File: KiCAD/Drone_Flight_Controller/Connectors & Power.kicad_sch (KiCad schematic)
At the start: 10 parts, among them J1 XT60, P1 USB_C_Plug_USB2.0, U4 AS358, U5 AS358

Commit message: Fix Bugs
Fix Bugs
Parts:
- removed U5: AS358, Package_SO:SO-8_3.9x4.9mm_P1.27mm, symbol Device:Opamp_Dual
- added U6: AS358, Package_SO:SO-8_3.9x4.9mm_P1.27mm, symbol Device:Opamp_Dual
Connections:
- net +14.8V: now also U6.8 (V+)
- net GND: now also U6.4 (V-)
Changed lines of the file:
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@@
+	)
+	(junction
+		(at 73.66 76.2)
+		(diameter 0)
+		(color 0 0 0 0)
 	)
 	(junction
@@
 	(wire
 		(pts
+			(xy 161.29 99.06) (xy 161.29 101.6)
+		)
+		(stroke
+			(width 0)
+			(type default)
+		)
+	)
+	(wire
+		(pts
 			(xy 142.24 81.28) (xy 152.4 81.28)
 		)
@@
 	(wire
 		(pts
+			(xy 161.29 83.82) (xy 161.29 81.28)
+		)
+		(stroke
+			(width 0)
+			(type default)
+		)
+	)
+	(wire
+		(pts
 			(xy 120.65 144.78) (xy 120.65 142.24)
 		)
@@
 	(wire
 		(pts
-			(xy 161.29 101.6) (xy 161.29 99.06)
-		)
-		(stroke
-			(width 0)
-			(type default)
-		)
-	)
-	(wire
-		(pts
 			(xy 71.12 83.82) (xy 73.66 83.82)
 		)
@@
 	(wire
 		(pts
-			(xy 161.29 83.82) (xy 161.29 81.28)
-		)
-		(stroke
-			(width 0)
-			(type default)
-		)
-	)
-	(wire
-		(pts
 			(xy 71.12 93.98) (xy 73.66 93.98)
 		)
@@
 		(pts
 			(xy 130.81 81.28) (xy 142.24 81.28)
+		)
+		(stroke
+			(width 0)
+			(type default)
+		)
+	)
+	(wire
+		(pts
+			(xy 81.28 73.66) (xy 81.28 76.2)
+		)
+		(stroke
+			(width 0)
+			(type default)
+		)
+	)
+	(wire
+		(pts
+			(xy 81.28 76.2) (xy 73.66 76.2)
 		)
 		(stroke
@@
 	)
 	(symbol
+		(lib_id "Device:Opamp_Dual")
+		(at 163.83 91.44 0)
+		(unit 3)
+		(exclude_from_sim no)
+		(in_bom yes)
+		(on_board yes)
+		(dnp no)
+		(fields_autoplaced yes)
+		(property "Reference" "U6"
+			(at 162.56 90.1699 0)
+			(effects
+				(font
+					(size 1.27 1.27)
+				)
+				(justify left)
+			)
+		)
+		(property "Value" "AS358"
+			(at 162.56 92.7099 0)
+			(effects
+				(font
+					(size 1.27 1.27)
+				)
+				(justify left)
+			)
+		)
+		(property "Footprint" "Package_SO:SO-8_3.9x4.9mm_P1.27mm"
+			(at 163.83 91.44 0)
+			(effects
+				(font
+					(size 1.27 1.27)
+				)
+				(hide yes)
+			)
+		)
+		(property "Datasheet" "~"
+			(at 163.83 91.44 0)
+			(effects
+				(font
+					(size 1.27 1.27)
+				)
+				(hide yes)
+			)
+		)
+		(property "Description" "Dual operational amplifier"
+			(at 163.83 91.44 0)
+			(effects
+				(font
+					(size 1.27 1.27)
+				)
+				(hide yes)
+			)
+		)
+		(property "Sim.Library" "${KICAD9_SYMBOL_DIR}/Simulation_SPICE.sp"
+			(at 163.83 91.44 0)
+			(effects
+				(font
+					(size 1.27 1.27)
+				)
+				(hide yes)
+			)
+		)
+		(property "Sim.Name" "kicad_builtin_opamp_dual"
+			(at 163.83 91.44 0)
+			(effects
+				(font
+					(size 1.27 1.27)
+				)
+				(hide yes)
+			)
+		)
+		(property "Sim.Device" "SUBCKT"
+			(at 163.83 91.44 0)
+			(effects
+				(font
+					(size 1.27 1.27)
+				)
+				(hide yes)
+			)
+		)
+		(property "Sim.Pins" "1=out1 2=in1- 3=in1+ 4=vee 5=in2+ 6=in2- 7=out2 8=vcc"
+			(at 163.83 91.44 0)
+			(effects
+				(font
+					(size 1.27 1.27)
+				)
+				(hide yes)
+			)
+		)
+		(property "Link" "https://www.mouser.at/ProductDetail/Diodes-Incorporated/AS358MTR-G1?qs=FKu9oBikfSlRUA%252BzgDv25w%3D%3D"
+			(at 163.83 91.44 0)
+			(effects
+				(font
+					(size 1.27 1.27)
+				)
+				(hide yes)
+			)
+		)
+		(pin "5"
+		)
+		(pin "6"
+		)
+		(pin "7"
+		)
+		(pin "1"
+		)
+		(pin "3"
+		)
+		(pin "8"
+		)
+		(pin "2"
+		)
+		(pin "4"
+		)
+		(instances
+			(project "Drone_Flight_Controller"
+				(path "/05daaa24-e506-4b9a-9564-8bf799413ca8/260564b2-f35d-47a6-9418-8c7c5bce9239"
+					(reference "U6")
+					(unit 3)
+				)
+			)
+		)
+	)
+	(symbol
 		(lib_id "power:PWR_FLAG")
 		(at 130.81 78.74 0)
@@
 	)
 	(symbol
+		(lib_id "power:PWR_FLAG")
+		(at 81.28 73.66 0)
+		(unit 1)
+		(exclude_from_sim no)
+		(in_bom yes)
+		(on_board yes)
+		(dnp no)
+		(fields_autoplaced yes)
+		(property "Reference" "#FLG04"
+			(at 81.28 71.755 0)
+			(effects
+				(font
+					(size 1.27 1.27)
+				)
+				(hide yes)
+			)
+		)
+		(property "Value" "PWR_FLAG"
+			(at 81.28 68.58 0)
+			(effects
+				(font
+					(size 1.27 1.27)
+				)
+			)
+		)
+		(property "Footprint" ""
+			(at 81.28 73.66 0)
+			(effects
+				(font
+					(size 1.27 1.27)
+				)
+				(hide yes)
+			)
+		)
+		(property "Datasheet" "~"
+			(at 81.28 73.66 0)
+			(effects
+				(font
+					(size 1.27 1.27)
+				)
+				(hide yes)
+			)
+		)
+		(property "Description" "Special symbol for telling ERC where power comes from"
+			(at 81.28 73.66 0)
+			(effects
+				(font
+					(size 1.27 1.27)
+				)
+				(hide yes)
+			)
+		)
+		(pin "1"
+		)
+		(instances
+			(project ""
+				(path "/05daaa24-e506-4b9a-9564-8bf799413ca8/260564b2-f35d-47a6-9418-8c7c5bce9239"
+					(reference "#FLG04")
+					(unit 1)
+				)
+			)
+		)
+	)
+	(symbol
 		(lib_id "Connector_Generic:Conn_01x02")
 		(at 109.22 92.71 180)
@@
 				)
 			)
-		)
-	)
-	(symbol
-		(lib_id "Device:Opamp_Dual")
-		(at 163.83 91.44 0)
-		(unit 3)
-		(exclude_from_sim no)
-		(in_bom yes)
-		(on_board yes)
-		(dnp no)
-		(fields_autoplaced yes)
-		(property "Reference" "U5"
-			(at 162.56 90.1699 0)
-			(effects
-				(font
-					(size 1.27 1.27)
-				)
-				(justify left)
-			)
-		)
-		(property "Value" "AS358"
-			(at 162.56 92.7099 0)
-			(effects
-				(font
-					(size 1.27 1.27)
-				)
-				(justify left)
-			)
-		)
-		(property "Footprint" "Package_SO:SO-8_3.9x4.9mm_P1.27mm"
-			(at 163.83 91.44 0)
-			(effects
-				(font
-					(size 1.27 1.27)
-				)
-				(hide yes)
-			)
-		)
-		(property "Datasheet" "https://www.mouser.at/datasheet/2/115/DIOD_S_A0005046231_1-2542568.pdf"
-			(at 163.83 91.44 0)
-			(effects
-				(font
-					(size 1.27 1.27)
-				)
-				(hide yes)
-			)
-		)
-		(property "Description" "Dual operational amplifier"
-			(at 163.83 91.44 0)
-			(effects
-				(font
-					(size 1.27 1.27)
-				)
-				(hide yes)
-			)
-		)
-		(property "Sim.Library" "${KICAD9_SYMBOL_DIR}/Simulation_SPICE.sp"
-			(at 163.83 91.44 0)
-			(effects
-				(font
-					(size 1.27 1.27)
-				)
-				(hide yes)
-			)
-		)
-		(property "Sim.Name" "kicad_builtin_opamp_dual"
-			(at 163.83 91.44 0)
-			(effects
-				(font
-					(size 1.27 1.27)
-				)
-				(hide yes)
-			)
-		)
-		(property "Sim.Device" "SUBCKT"
-			(at 163.83 91.44 0)
-			(effects
-				(font
-					(size 1.27 1.27)
-				)
-				(hide yes)
-			)
-		)
-		(property "Sim.Pins" "1=out1 2=in1- 3=in1+ 4=vee 5=in2+ 6=in2- 7=out2 8=vcc"
-			(at 163.83 91.44 0)
-			(effects
-				(font
-					(size 1.27 1.27)
-				)
-				(hide yes)
-			)
-		)
-		(property "Link" "https://www.mouser.at/ProductDetail/Diodes-Incorporated/AS358MTR-G1?qs=FKu9oBikfSlRUA%252BzgDv25w%3D%3D"
-			(at 163.83 91.44 0)
-			(effects
-				(font
-					(size 1.27 1.27)
-				)
-				(hide yes)
-			)
-		)
-		(pin "5"
-		)
-		(pin "6"
-		)
-		(pin "7"
-		)
-		(pin "1"
-		)
-		(pin "3"
-		)
-		(pin "8"
-		)
-		(pin "2"
-		)
-		(pin "4"
-		)
-		(instances
-			(project "Drone_Flight_Controller"
-				(path "/05daaa24-e506-4b9a-9564-8bf799413ca8/260564b2-f35d-47a6-9418-8c7c5bce9239"
-					(reference "U5")
-					(unit 3)
-				)
-			)

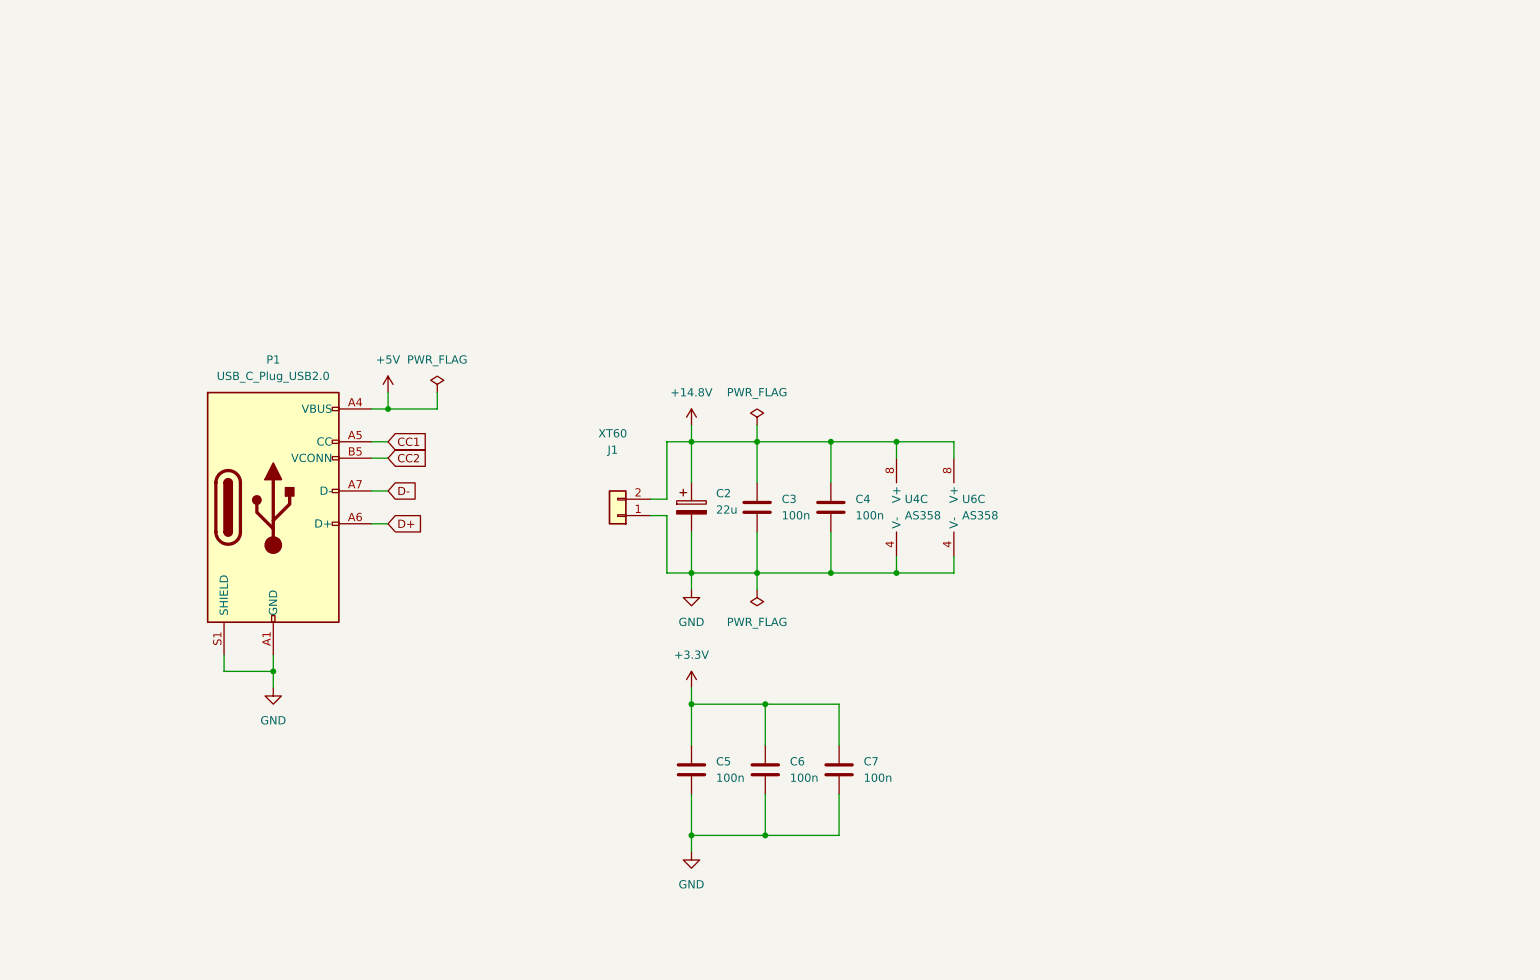
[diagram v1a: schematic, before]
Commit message: Change +14.8V & GND to +BATT & -BATT
Change +14.8V& GND to +BATT & -BATT
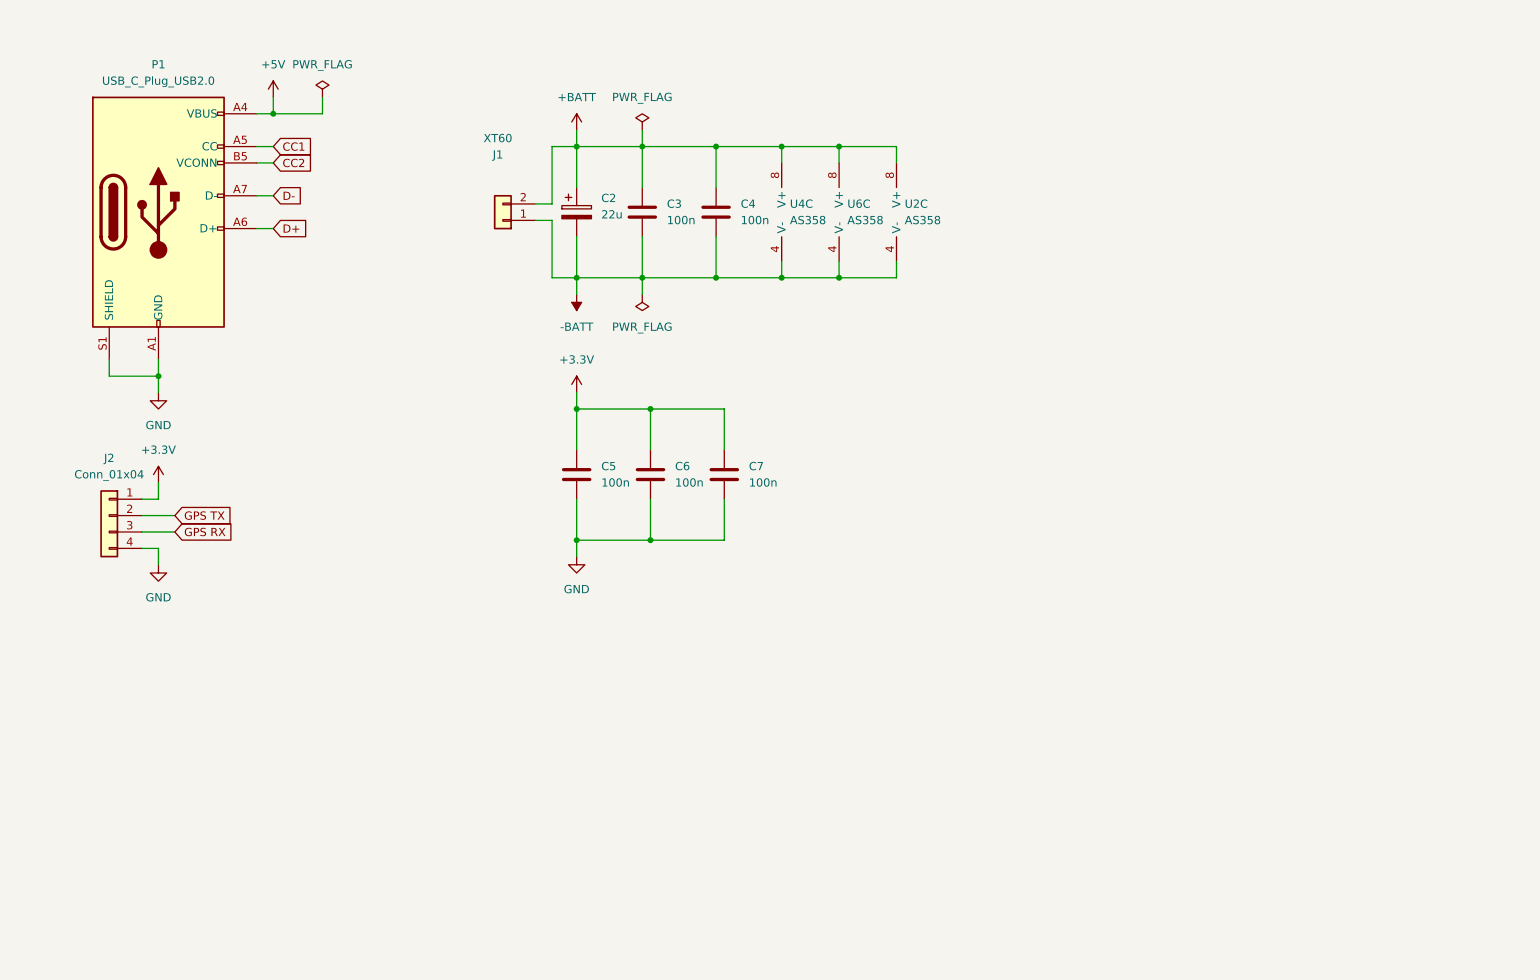
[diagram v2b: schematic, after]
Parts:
- added J2: Conn_01x04, symbol Connector_Generic:Conn_01x04
- added U2: AS358, Package_SO:SO-8_3.9x4.9mm_P1.27mm, symbol Device:Opamp_Dual
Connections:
- net +3.3V: now also J2.1 (Pin_1)
- net GND: now also J2.4 (Pin_4); no longer C2.2, C3.2, C4.2, J1.1 (Pin_1), U4.4 (V-), U6.4 (V-)
- net +14.8V renamed +BATT
- net +BATT: now also U2.8 (V+)
- new net -BATT: C2.2, C3.2, C4.2, J1.1 (Pin_1), U2.4 (V-), U4.4 (V-), U6.4 (V-)
- new net GPS RX: J2.3 (Pin_3)
- new net GPS TX: J2.2 (Pin_2)
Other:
- moved on the sheet: C2, C3, C4, C5, C6, C7, J1, P1, U4C, U6C

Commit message: Move USB to USB & Status LEDs. Add ESC Drive circuits
Move USB to USB & Status LEDs. Add ESC Drive circuits
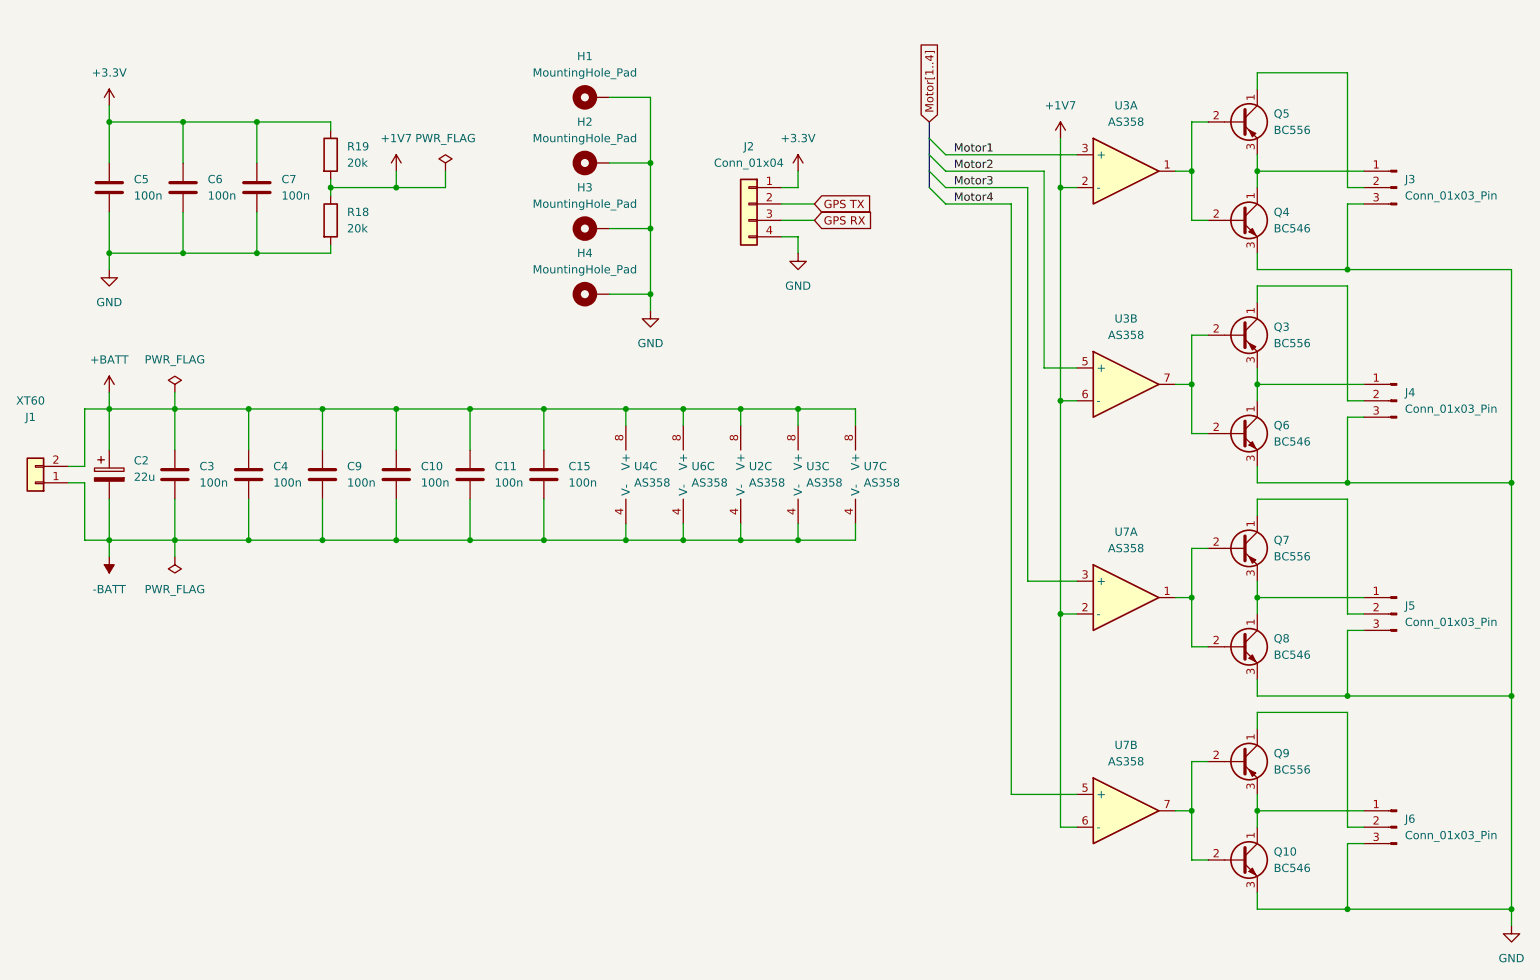
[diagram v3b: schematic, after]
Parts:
- removed P1: USB_C_Plug_USB2.0, symbol Connector:USB_C_Plug_USB2.0
- added C10, C11, C15, C9: 100n, Capacitor_SMD:C_0805_2012Metric_Pad1.18x1.45mm_HandSolder, symbol Device:C
- added H1, H2, H3, H4: MountingHole_Pad, MountingHole:MountingHole_3.2mm_M3_Pad_TopBottom, symbol Mechanical:MountingHole_Pad
- added J3, J4, J5, J6: Conn_01x03_Pin, Connector_PinHeader_2.54mm:PinHeader_1x04_P2.54mm_Vertical, symbol Connector:Conn_01x03_Pin
- added Q10, Q4, Q6, Q8: BC546, Package_TO_SOT_THT:TO-92_Inline, symbol Transistor_BJT:BC546
- added Q3, Q5, Q7, Q9: BC556, Package_TO_SOT_THT:TO-92_Inline, symbol Transistor_BJT:BC556
- added R18, R19: 20k, Resistor_SMD:R_0805_2012Metric_Pad1.20x1.40mm_HandSolder, symbol Device:R
- added U3, U7: AS358, Package_SO:SO-8_3.9x4.9mm_P1.27mm, symbol Device:Opamp_Dual
- J2: footprint (none) -> Connector_PinHeader_2.54mm:PinHeader_1x04_P2.54mm_Vertical; Link (none) -> /
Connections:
- net +3.3V: now also R19.1
- net +BATT: now also C10.1, C11.1, C15.1, C9.1, U3.8 (V+), U7.8 (V+)
- net -BATT: now also C10.2, C11.2, C15.2, C9.2, U3.4 (V-), U7.4 (V-)
- net GND: now also H1.1, H2.1, H3.1, H4.1, J3.3 (Pin_3), J4.3 (Pin_3), J5.3 (Pin_3), J6.3 (Pin_3), Q10.3 (E), Q4.3 (E), Q6.3 (E), Q8.3 (E), R18.2
- new net: J4.1 (Pin_1), Q3.3 (E), Q6.1 (C)
- new net: Q3.2 (B), Q6.2 (B), U3.7
- new net: Q7.2 (B), Q8.2 (B), U7.1
- new net: Q10.2 (B), Q9.2 (B), U7.7
- new net: J3.1 (Pin_1), Q4.1 (C), Q5.3 (E)
- new net: Q4.2 (B), Q5.2 (B), U3.1
- new net: J6.1 (Pin_1), Q10.1 (C), Q9.3 (E)
- new net: J6.2 (Pin_2), Q9.1 (C)
- new net: J4.2 (Pin_2), Q3.1 (C)
- new net: J3.2 (Pin_2), Q5.1 (C)
- new net: J5.2 (Pin_2), Q7.1 (C)
- new net: J5.1 (Pin_1), Q7.3 (E), Q8.1 (C)
- new net +1V7: R18.1, R19.2, U3.2 (-), U3.6 (-), U7.2 (-), U7.6 (-)
- new net Motor1: U3.3 (+)
- new net Motor2: U3.5 (+)
- new net Motor3: U7.3 (+)
- new net Motor4: U7.5 (+)
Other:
- moved on the sheet: C2, C3, C4, C5, C6, C7, J1, J2, U2C, U4C, U6C

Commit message: Fix Footprint Error
Fix Footprint Error
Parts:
- J3, J4, J5, J6: footprint Connector_PinHeader_2.54mm:PinHeader_1x04_P2.54mm_Vertical -> Connector_PinHeader_2.54mm:PinHeader_1x03_P2.54mm_Vertical
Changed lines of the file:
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@@
 			)
 		)
-		(property "Footprint" "Connector_PinHeader_2.54mm:PinHeader_1x04_P2.54mm_Vertical"
+		(property "Footprint" "Connector_PinHeader_2.54mm:PinHeader_1x03_P2.54mm_Vertical"
 			(at 229.87 140.97 0)
 			(effects
@@
 			)
 		)
-		(property "Footprint" "Connector_PinHeader_2.54mm:PinHeader_1x04_P2.54mm_Vertical"
+		(property "Footprint" "Connector_PinHeader_2.54mm:PinHeader_1x03_P2.54mm_Vertical"
 			(at 229.87 74.93 0)
 			(effects
@@
 			)
 		)
-		(property "Footprint" "Connector_PinHeader_2.54mm:PinHeader_1x04_P2.54mm_Vertical"
+		(property "Footprint" "Connector_PinHeader_2.54mm:PinHeader_1x03_P2.54mm_Vertical"
 			(at 229.87 41.91 0)
 			(effects
@@
 			)
 		)
-		(property "Footprint" "Connector_PinHeader_2.54mm:PinHeader_1x04_P2.54mm_Vertical"
+		(property "Footprint" "Connector_PinHeader_2.54mm:PinHeader_1x03_P2.54mm_Vertical"
 			(at 229.87 107.95 0)
 			(effects

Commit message: Reanotate
Reanotate
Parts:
- renumbered C5 to C301, C2 to C302, C3 to C303, C6 to C304, C4 to C305, C7 to C306, C9 to C307, C10 to C308, C11 to C309, C15 to C310, H1 to H301, H2 to H302, H3 to H303, H4 to H304, J1 to J301, J2 to J302, J3 to J303, J4 to J304, J5 to J305, J6 to J306, Q5 to Q301, Q4 to Q302, Q3 to Q303, Q6 to Q304, Q7 to Q305, Q8 to Q306, Q9 to Q307, Q10 to Q308, R19 to R301, R18 to R302, U4 to U202, U6 to U203, U2 to U301, U3 to U302, U7 to U303

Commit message: Fix Bypass Capacitor error
Fix Bypass Capacitor error
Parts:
- renumbered C304 to C302, C306 to C303, C310 to C304, C302 to C305, C303 to C306, C305 to C307, C307 to C308, C308 to C309, C309 to C310, J303 to J301, J304 to J303, J301 to J304, U202 to U301, U203 to U303, U301 to U304, U303 to U305
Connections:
- net +3.3V: now also C304.1
- net +BATT: no longer C304.1
- net -BATT: no longer C304.2
- net GND: now also C304.2
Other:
- moved on the sheet: C304, R301, R302

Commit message: Reannotate
Reannotate
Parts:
- renumbered U301 to U202, U303 to U203, U302 to U301, U304 to U302
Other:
- moved on the sheet: U202C, U203C, U301C, U302C, U305C
